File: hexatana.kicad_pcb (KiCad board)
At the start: 2 copper layers, 279.5 x 98.2 mm, 66 parts, among them J1 USB_C_Receptacle_USB2.0, SW1 SW_Push, SW10 SW_Push, SW11 SW_Push, SW12 SW_Push, SW13 SW_Push, SW14 SW_Push, SW15 SW_Push, SW16 SW_Push, SW17 SW_Push, SW18 SW_Push, SW19 SW_Push, SW2 SW_Push, SW20 SW_Push, SW21 SW_Push, SW22 SW_Push, SW23 SW_Push, SW24 SW_Push, SW25 SW_Push, SW26 SW_Push, SW27 SW_Push, SW28 SW_Push, SW29 SW_Push, SW3 SW_Push, SW30 SW_Push, SW31 SW_Push, SW32 SW_Push, SW33 SW_Push, SW34 SW_Push, SW35 BOOT, SW36 RESET, SW37 SW_Push, SW38 SW_Push, SW4 SW_Push, SW5 SW_Push, SW6 SW_Push, SW7 SW_Push, SW8 SW_Push, SW9 SW_Push, U2 USBLC6-2SC6

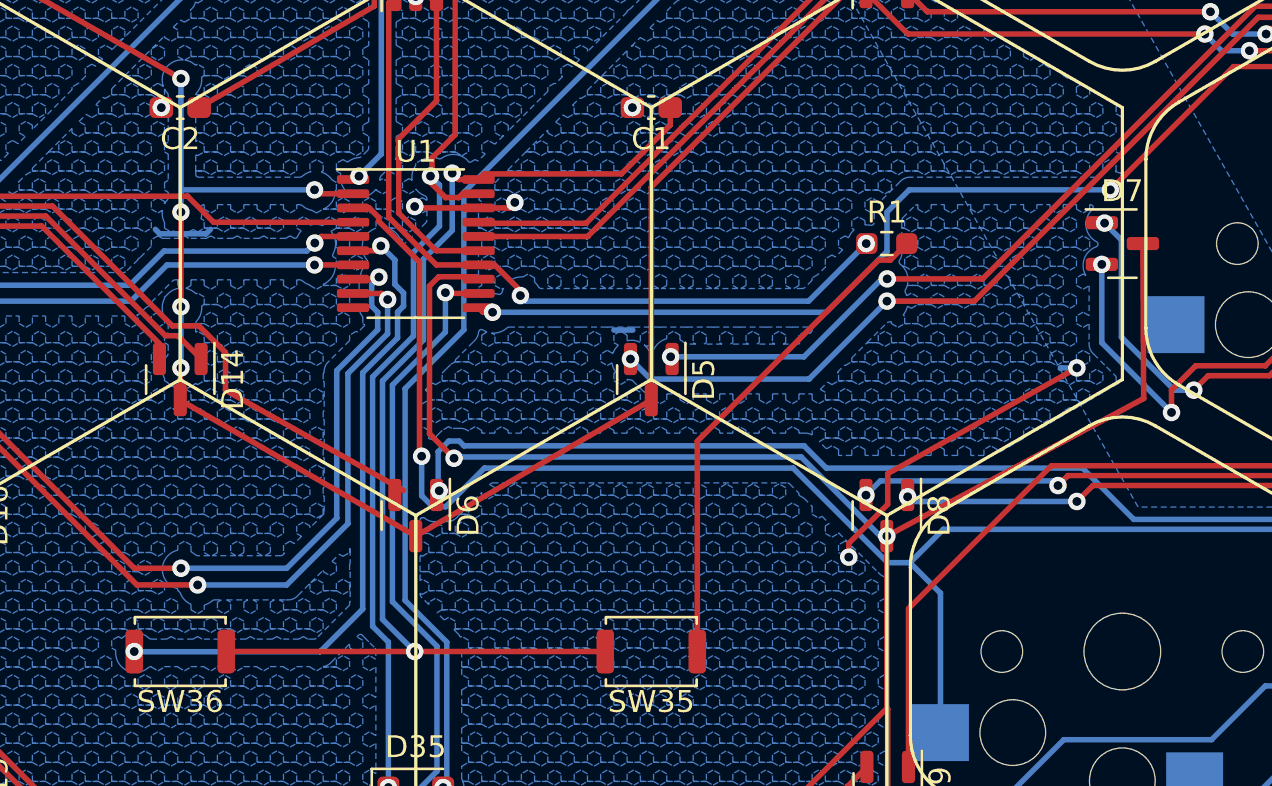
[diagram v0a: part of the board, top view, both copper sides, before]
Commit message: fixed missing col5 on mcu
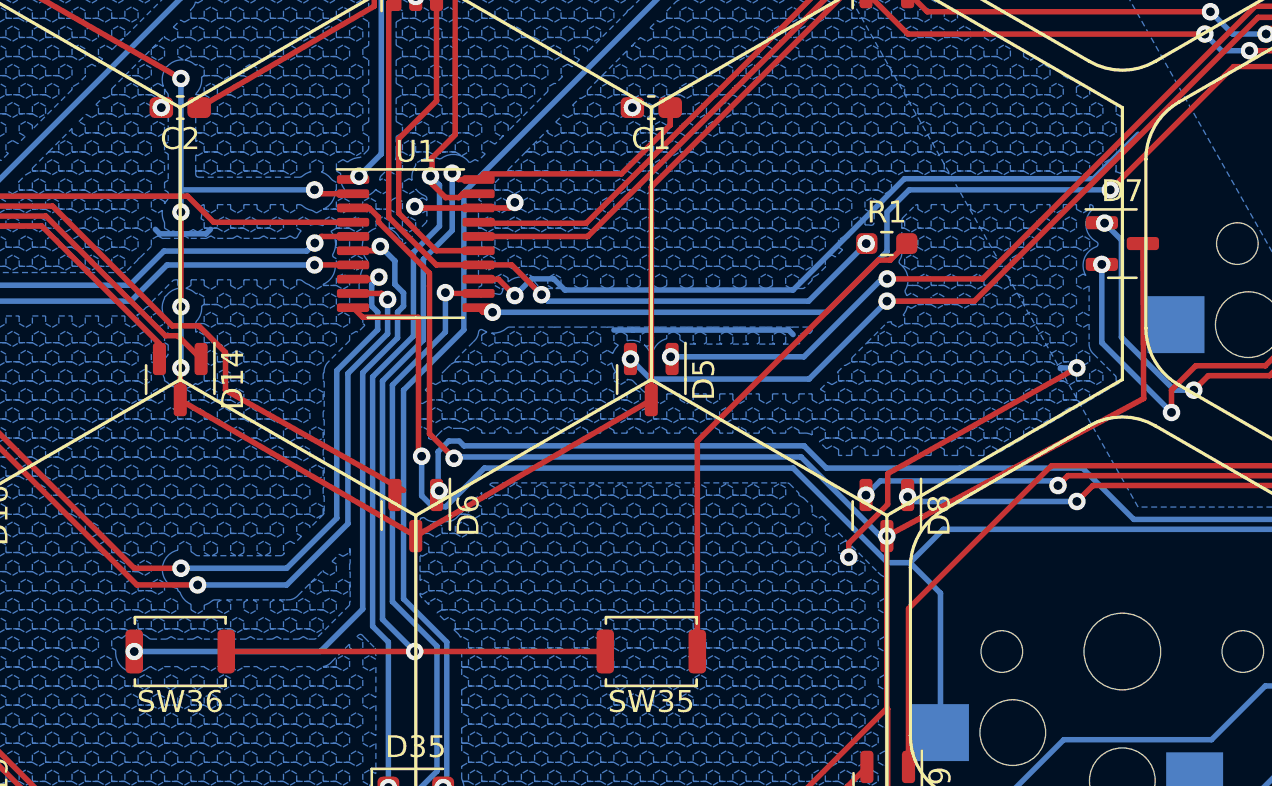
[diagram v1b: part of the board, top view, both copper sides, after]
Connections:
- U1 pad 10: P3.0_RX -> col4
- U1 pad 13: row3 -> col5
- U1 pad 3: col4 -> row3
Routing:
- net col5: track 53.4 -> 87.3 mm, vias 4 -> 5
- net GND: track 70.0 -> 77.4 mm
- net col4: track 81.9 -> 78.4 mm
- net row3: track 139.4 -> 142.4 mm
